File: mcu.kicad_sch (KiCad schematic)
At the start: 31 parts, among them J1 SM03B-SRSS-TB, SW1 SW_Push, SW2 SW_Push, U1 RP2350_60QFN, U2 W25Q128JVS, Y1 ABM8-272-T3

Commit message: add user led schematic
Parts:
- added D6: BLUE, LED_SMD:LED_0603_1608Metric, symbol Device:LED
- added R38: 1k, Resistor_SMD:R_0603_1608Metric, symbol Device:R
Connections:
- net GND: now also R38.2
- net at U1.36 (GPIO24): now also D6.2 (A)
- new net: D6.1 (K), R38.1
- no-connect marks 7 -> 6

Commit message: custom sideways led footprint
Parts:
- D6: footprint LED_SMD:LED_0603_1608Metric -> RP2350_60QFN_minimal:LED_Sideways
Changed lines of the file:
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@@
 			)
 		)
-		(property "Footprint" "LED_SMD:LED_0603_1608Metric"
+		(property "Footprint" "RP2350_60QFN_minimal:LED_Sideways"
 			(at 189.23 146.05 0)
 			(hide yes)

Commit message: changed amp sd_mode resistor value, move caps, add i2c pullups
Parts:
- added R40, R41: 5.1k, Resistor_SMD:R_0603_1608Metric, symbol Device:R
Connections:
- net +3V3: now also R40.1, R41.1
- net POWER_MON_SCL: now also R40.2
- net POWER_MON_SDA: now also R41.2
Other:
- note added: "I^{2}C pullups"

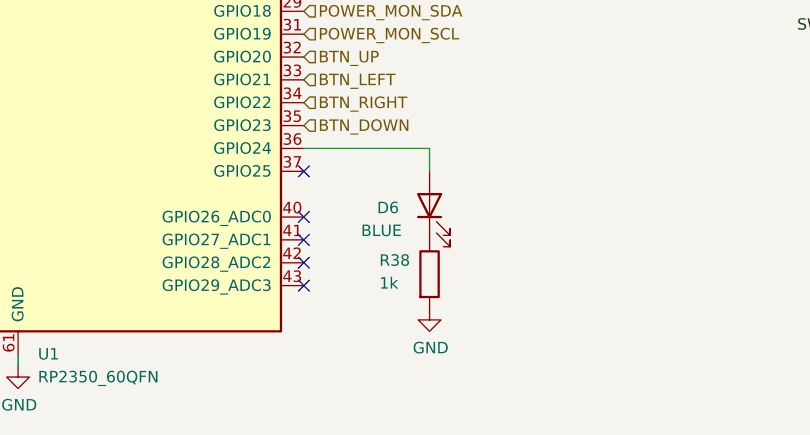
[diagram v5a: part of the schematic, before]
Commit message: update components
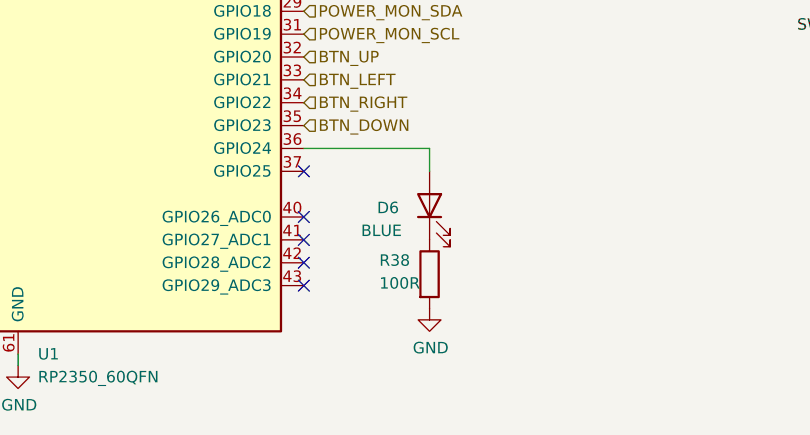
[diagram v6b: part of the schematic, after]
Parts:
- R38: value 1k -> 100R; LCSC (none) -> C22775; Manufacturer (none) -> UNI-ROYAL(Uniroyal Elec); Manufacturer Part Number (none) -> 0603WAF1000T5E
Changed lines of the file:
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@@
 			)
 		)
-		(property "Value" "1k"
+		(property "Value" "100R"
 			(at 183.642 154.686 0)
 			(show_name no)
@@
 			)
 		)
-		(property "LCSC" ""
+		(property "LCSC" "C22775"
 			(at 189.23 153.67 0)
 			(hide yes)
@@
 			)
 		)
-		(property "Manufacturer" ""
+		(property "Manufacturer" "UNI-ROYAL(Uniroyal Elec)"
 			(at 189.23 153.67 0)
 			(hide yes)
@@
 			)
 		)
-		(property "Manufacturer Part Number" ""
+		(property "Manufacturer Part Number" "0603WAF1000T5E"
 			(at 189.23 153.67 0)
 			(hide yes)
